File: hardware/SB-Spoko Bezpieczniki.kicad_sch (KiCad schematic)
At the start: 23 parts, among them IC1 STM32L4P5RET6, SW1 RESET, Y1 Crystal_GND24_Small

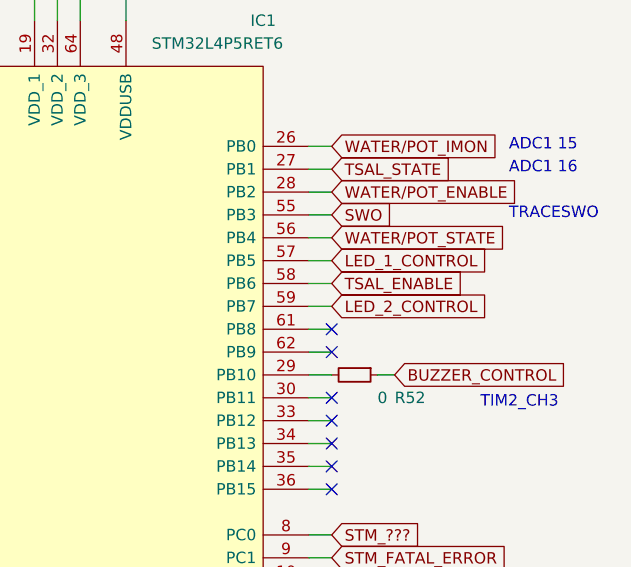
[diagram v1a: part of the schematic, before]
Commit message: currected TSAL, cause it can't be controled via external logic
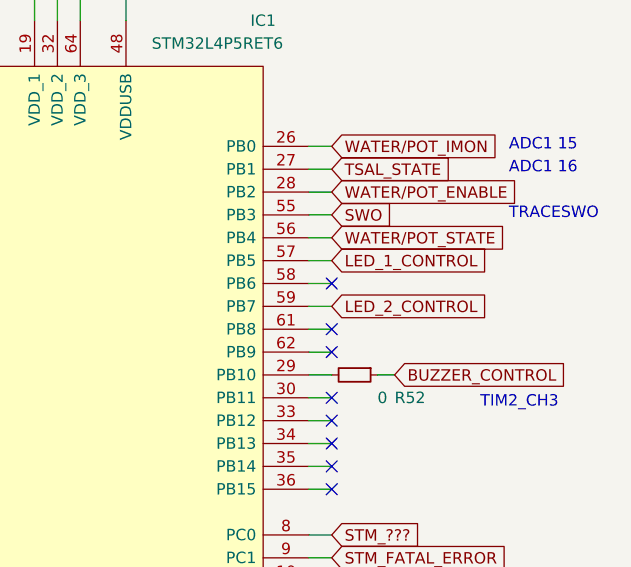
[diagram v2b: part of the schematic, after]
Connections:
- net TSAL_ENABLE: no longer names the net of IC1.58 (PB6)
- no-connect marks 15 -> 16
